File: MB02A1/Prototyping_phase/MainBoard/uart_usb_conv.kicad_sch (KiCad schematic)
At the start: 45 parts, among them J1 USB_B_Mini, J2 USB_B_Mini, J3 USB_B_Mini, U1 CH340G, U2 CH340G, U3 CH340G, X1 12MHz, X2 12MHz, X3 12MHz

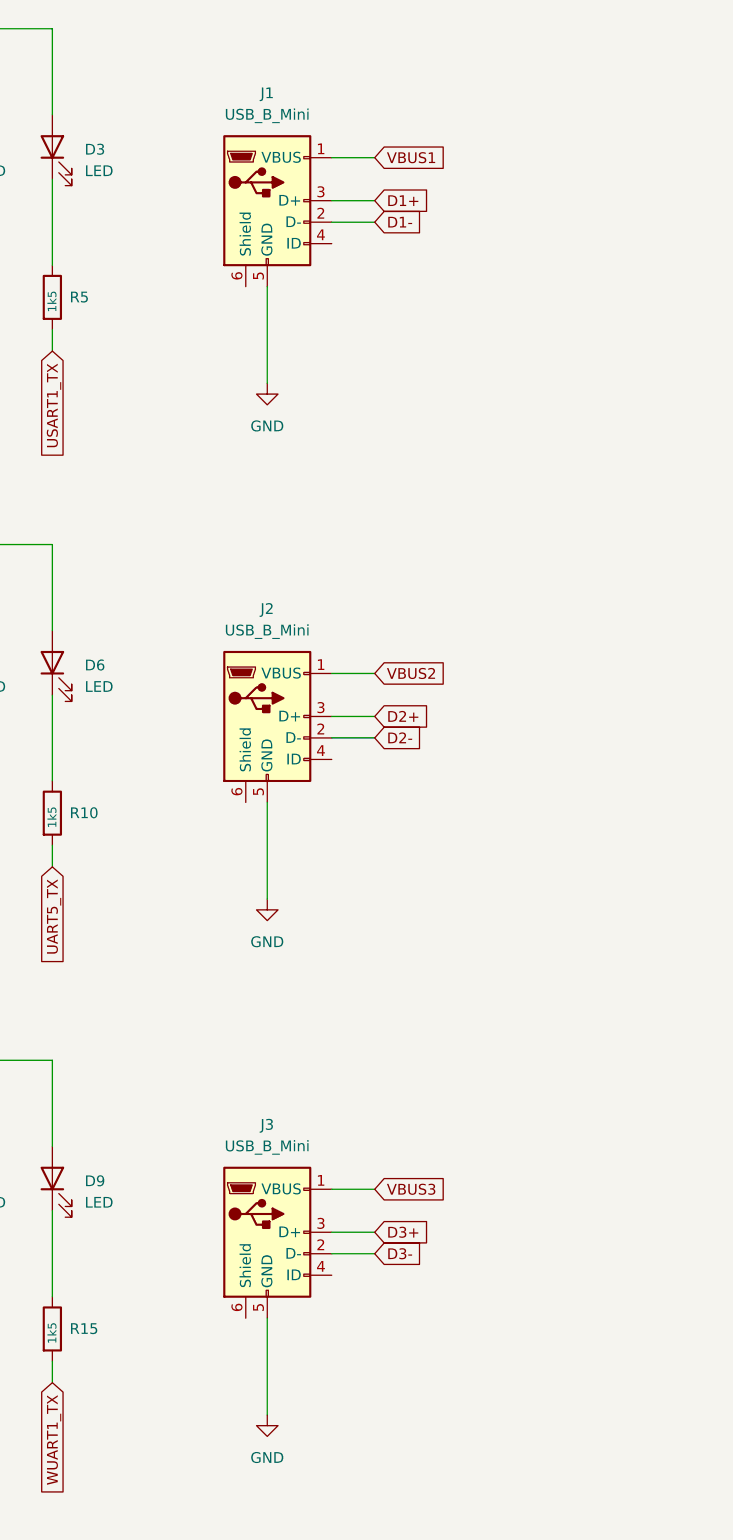
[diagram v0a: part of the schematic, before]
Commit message: Datasheets added, design updated.
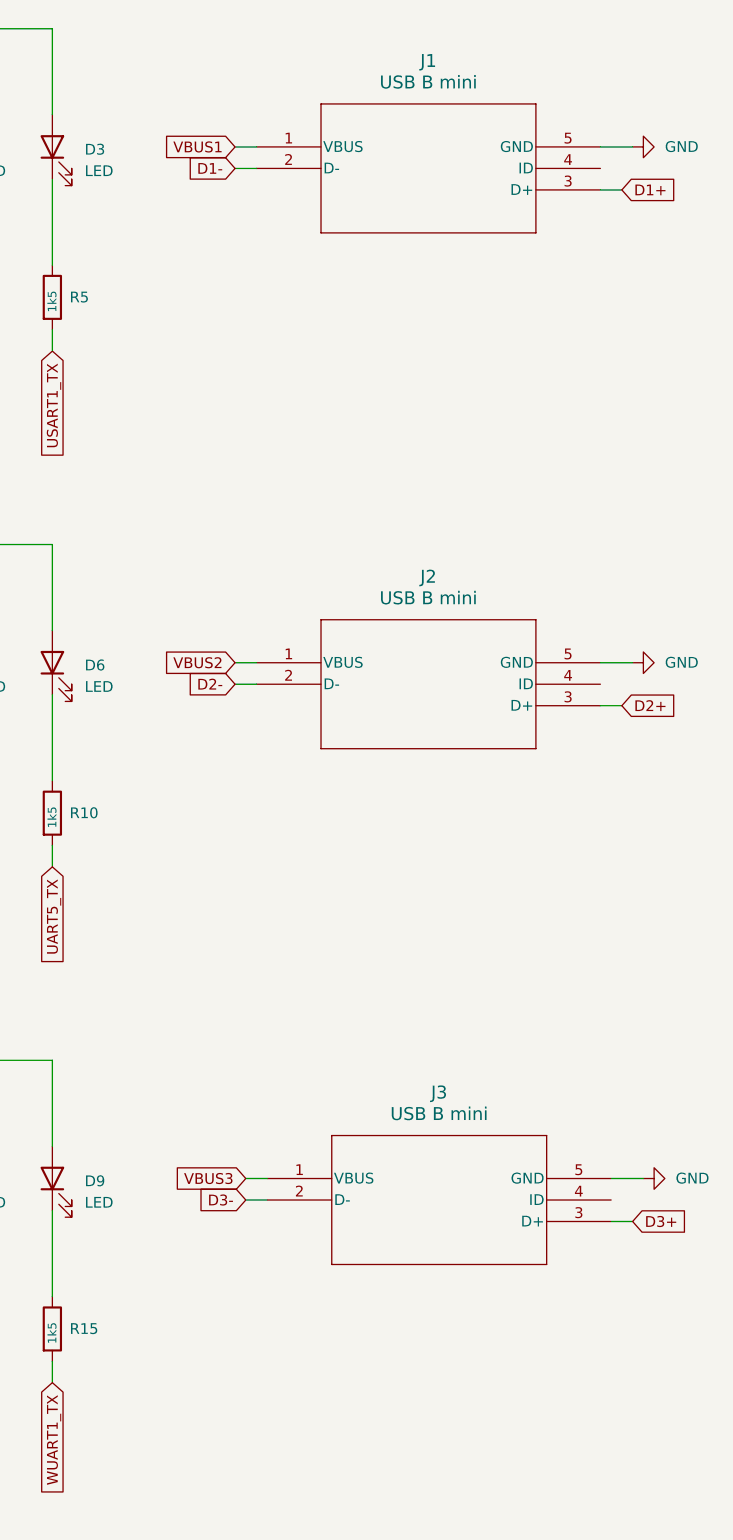
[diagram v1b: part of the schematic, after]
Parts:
- removed J1, J2, J3: USB_B_Mini, Connector_USB:USB_Mini-B_Wuerth_65100516121_Horizontal, symbol Connector:USB_B_Mini
- added J1, J2, J3: USB B mini, 54819-0519_MOL, symbol USB_B_mini_th:548190519
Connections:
- net D1+: now also J1.3 (D+)
- net D1-: now also J1.2 (D-)
- net D2+: now also J2.3 (D+)
- net D2-: now also J2.2 (D-)
- net D3+: now also J3.3 (D+)
- net D3-: now also J3.2 (D-)
- net GND: now also J1.5 (GND), J2.5 (GND), J3.5 (GND)
- net VBUS1: now also J1.1 (VBUS)
- net VBUS2: now also J2.1 (VBUS)
- net VBUS3: now also J3.1 (VBUS)

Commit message: Design update, production preparation.
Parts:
- X1, X2, X3: value 12MHz -> 12 MHz; footprint Crystal:Crystal_HC18-U_Vertical -> Crystal:Crystal_HC49-U_Vertical
- renumbered C11 to C10, C4 to C11, C8 to C12, C12 to C13, C1 to C2, C5 to C3, C9 to C4, C2 to C5, C10 to C7, C3 to C8, C7 to C9, D3 to D10, D6 to D11, D9 to D12, D1 to D4, D4 to D5, D7 to D6, D2 to D7, D5 to D8, D8 to D9, J1 to J2, J2 to J3, J3 to J4, R12 to R10, R3 to R11, R8 to R12, R4 to R14, R9 to R15, R14 to R16, R5 to R17, R10 to R18, R15 to R19, R1 to R5, R2 to R6, R6 to R7, R7 to R8, R11 to R9, U1 to U2, U2 to U3, U3 to U4
